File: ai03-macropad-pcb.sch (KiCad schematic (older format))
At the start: 74 parts, among them J1 Conn_01x06, SW1 SW_Push, U1 ATmega32U4-MU, Y1 16Mhz

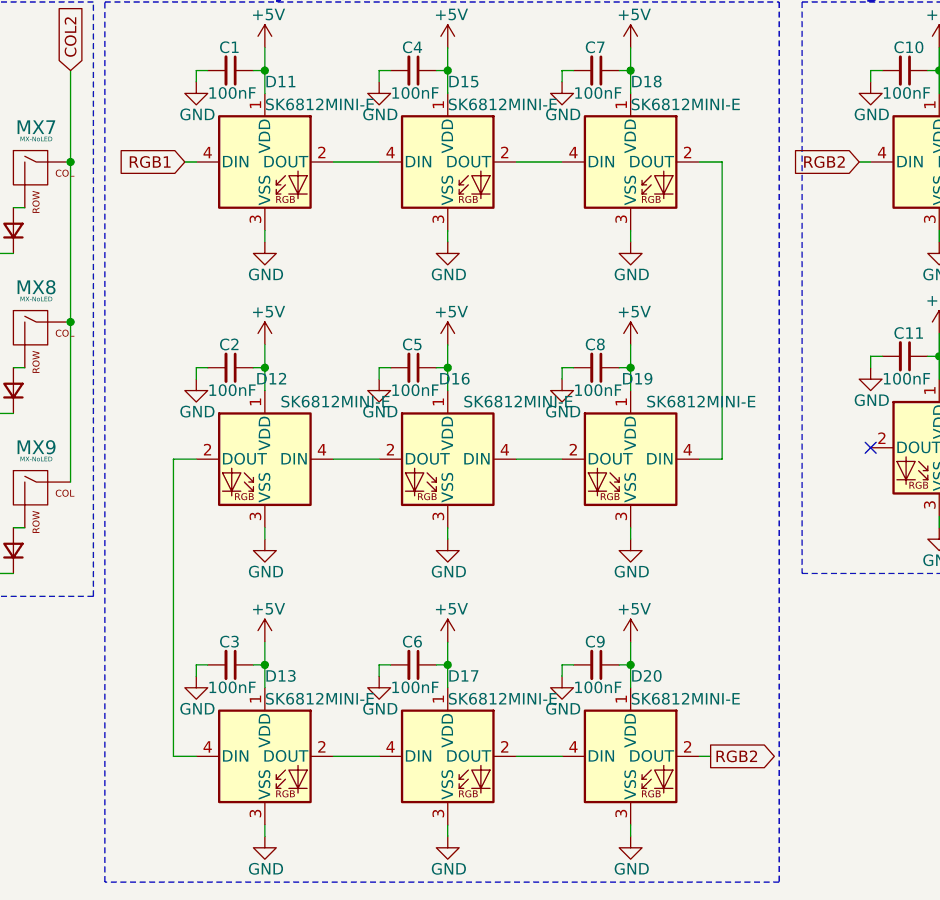
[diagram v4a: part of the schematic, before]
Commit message: Routing for switches and RGBs
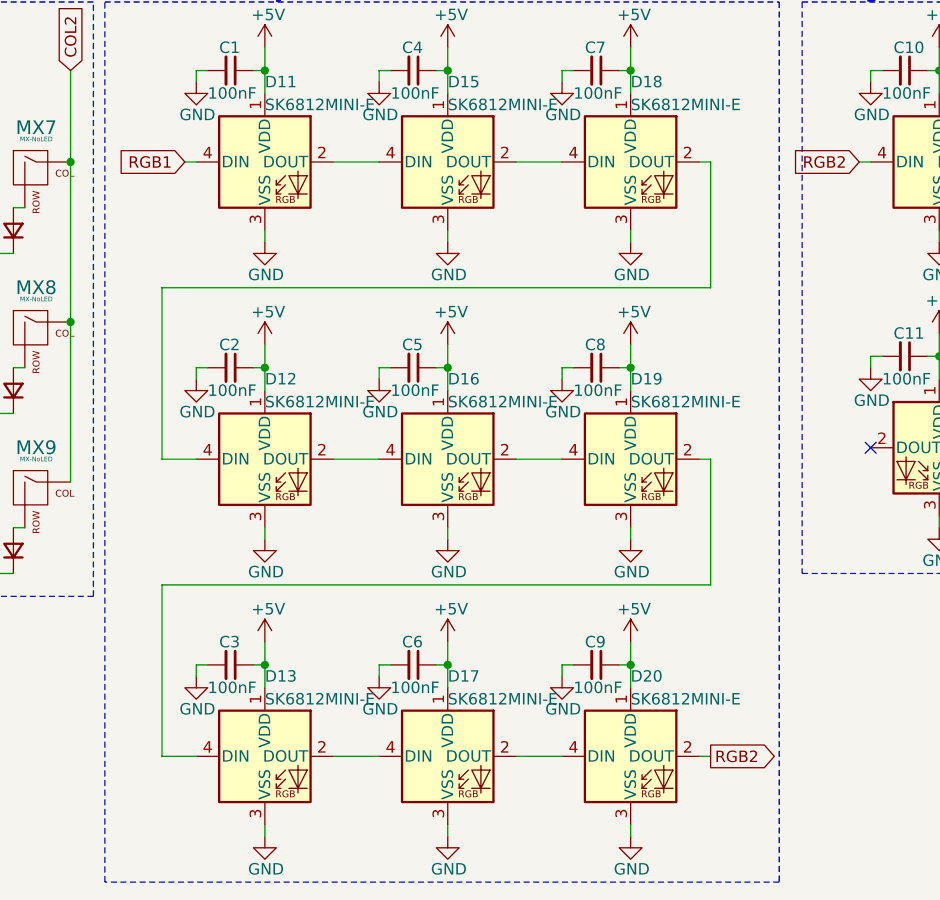
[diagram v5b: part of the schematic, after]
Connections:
- net at D18.2 (DOUT): now also D12.4 (DIN); no longer D19.4 (DIN)
- net at D19.2 (DOUT): now also D13.4 (DIN); no longer D16.4 (DIN)
- net at D16.2 (DOUT): now also D19.4 (DIN); no longer D12.4 (DIN)
- net at D12.2 (DOUT): now also D16.4 (DIN); no longer D13.4 (DIN)
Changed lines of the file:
@@
 	4400 4600 4600 4600
-Wire Wire Line
-	5200 4600 5300 4600
-Wire Wire Line
-	5300 4600 5300 5900
-Wire Wire Line
-	5300 5900 5200 5900
-Wire Wire Line
-	4600 5900 4400 5900
-Wire Wire Line
-	3800 5900 3600 5900
-Wire Wire Line
-	3000 5900 2900 5900
-Wire Wire Line
-	2900 5900 2900 7200
-Wire Wire Line
-	2900 7200 3000 7200
 Wire Wire Line
 	3600 7200 3800 7200
@@
 	1    4900 4600
 	1    0    0    -1
-$EndComp
-$Comp
-L kicad-keyboard-parts:SK6812MINI-E D19
-U 1 1 60741DD2
-P 4900 5900
-F 0 "D19" H 4800 6250 50  0000 L CNN
-F 1 "SK6812MINI-E" H 4350 6150 50  0000 L CNN
-F 2 "kicad-keyboard-parts:MX_SK6812MINI-E" H 4950 5600 50  0001 L TNN
-F 3 "https://cdn-shop.adafruit.com/product-files/2686/SK6812MINI_REV.01-1-2.pdf" H 5000 5525 50  0001 L TNN
-	1    4900 5900
-	-1   0    0    -1
-$EndComp
-$Comp
-L kicad-keyboard-parts:SK6812MINI-E D16
-U 1 1 60750D73
-P 4100 5900
-F 0 "D16" H 4000 6250 50  0000 L CNN
-F 1 "SK6812MINI-E" H 3550 6150 50  0000 L CNN
-F 2 "kicad-keyboard-parts:MX_SK6812MINI-E" H 4150 5600 50  0001 L TNN
-F 3 "https://cdn-shop.adafruit.com/product-files/2686/SK6812MINI_REV.01-1-2.pdf" H 4200 5525 50  0001 L TNN
-	1    4100 5900
-	-1   0    0    -1
-$EndComp
-$Comp
-L kicad-keyboard-parts:SK6812MINI-E D12
-U 1 1 60751636
-P 3300 5900
-F 0 "D12" H 3200 6250 50  0000 L CNN
-F 1 "SK6812MINI-E" H 2750 6150 50  0000 L CNN
-F 2 "kicad-keyboard-parts:MX_SK6812MINI-E" H 3350 5600 50  0001 L TNN
-F 3 "https://cdn-shop.adafruit.com/product-files/2686/SK6812MINI_REV.01-1-2.pdf" H 3400 5525 50  0001 L TNN
-	1    3300 5900
-	-1   0    0    -1
 $EndComp
 $Comp
@@
 Text GLabel 10750 6000 2    50   Input ~ 0
 ROW2
+$Comp
+L kicad-keyboard-parts:SK6812MINI-E D12
+U 1 1 60761311
+P 3300 5900
+F 0 "D12" H 3300 6250 50  0000 L CNN
+F 1 "SK6812MINI-E" H 3300 6150 50  0000 L CNN
+F 2 "kicad-keyboard-parts:MX_SK6812MINI-E" H 3350 5600 50  0001 L TNN
+F 3 "https://cdn-shop.adafruit.com/product-files/2686/SK6812MINI_REV.01-1-2.pdf" H 3400 5525 50  0001 L TNN
+	1    3300 5900
+	1    0    0    -1
+$EndComp
+$Comp
+L kicad-keyboard-parts:SK6812MINI-E D16
+U 1 1 6076131B
+P 4100 5900
+F 0 "D16" H 4100 6250 50  0000 L CNN
+F 1 "SK6812MINI-E" H 4100 6150 50  0000 L CNN
+F 2 "kicad-keyboard-parts:MX_SK6812MINI-E" H 4150 5600 50  0001 L TNN
+F 3 "https://cdn-shop.adafruit.com/product-files/2686/SK6812MINI_REV.01-1-2.pdf" H 4200 5525 50  0001 L TNN
+	1    4100 5900
+	1    0    0    -1
+$EndComp
+$Comp
+L kicad-keyboard-parts:SK6812MINI-E D19
+U 1 1 60761325
+P 4900 5900
+F 0 "D19" H 4900 6250 50  0000 L CNN
+F 1 "SK6812MINI-E" H 4900 6150 50  0000 L CNN
+F 2 "kicad-keyboard-parts:MX_SK6812MINI-E" H 4950 5600 50  0001 L TNN
+F 3 "https://cdn-shop.adafruit.com/product-files/2686/SK6812MINI_REV.01-1-2.pdf" H 5000 5525 50  0001 L TNN
+	1    4900 5900
+	1    0    0    -1
+$EndComp
+Wire Wire Line
+	5200 4600 5250 4600
+Wire Wire Line
+	5250 4600 5250 5150
+Wire Wire Line
+	5250 5150 2850 5150
+Wire Wire Line
+	2850 5150 2850 5900
+Wire Wire Line
+	2850 5900 3000 5900
+Wire Wire Line
+	3600 5900 3800 5900
+Wire Wire Line
+	4400 5900 4600 5900
+Wire Wire Line
+	5200 5900 5250 5900
+Wire Wire Line
+	5250 5900 5250 6450
+Wire Wire Line
+	5250 6450 2850 6450
+Wire Wire Line
+	2850 6450 2850 7200
+Wire Wire Line
+	2850 7200 3000 7200
 $EndSCHEMATC

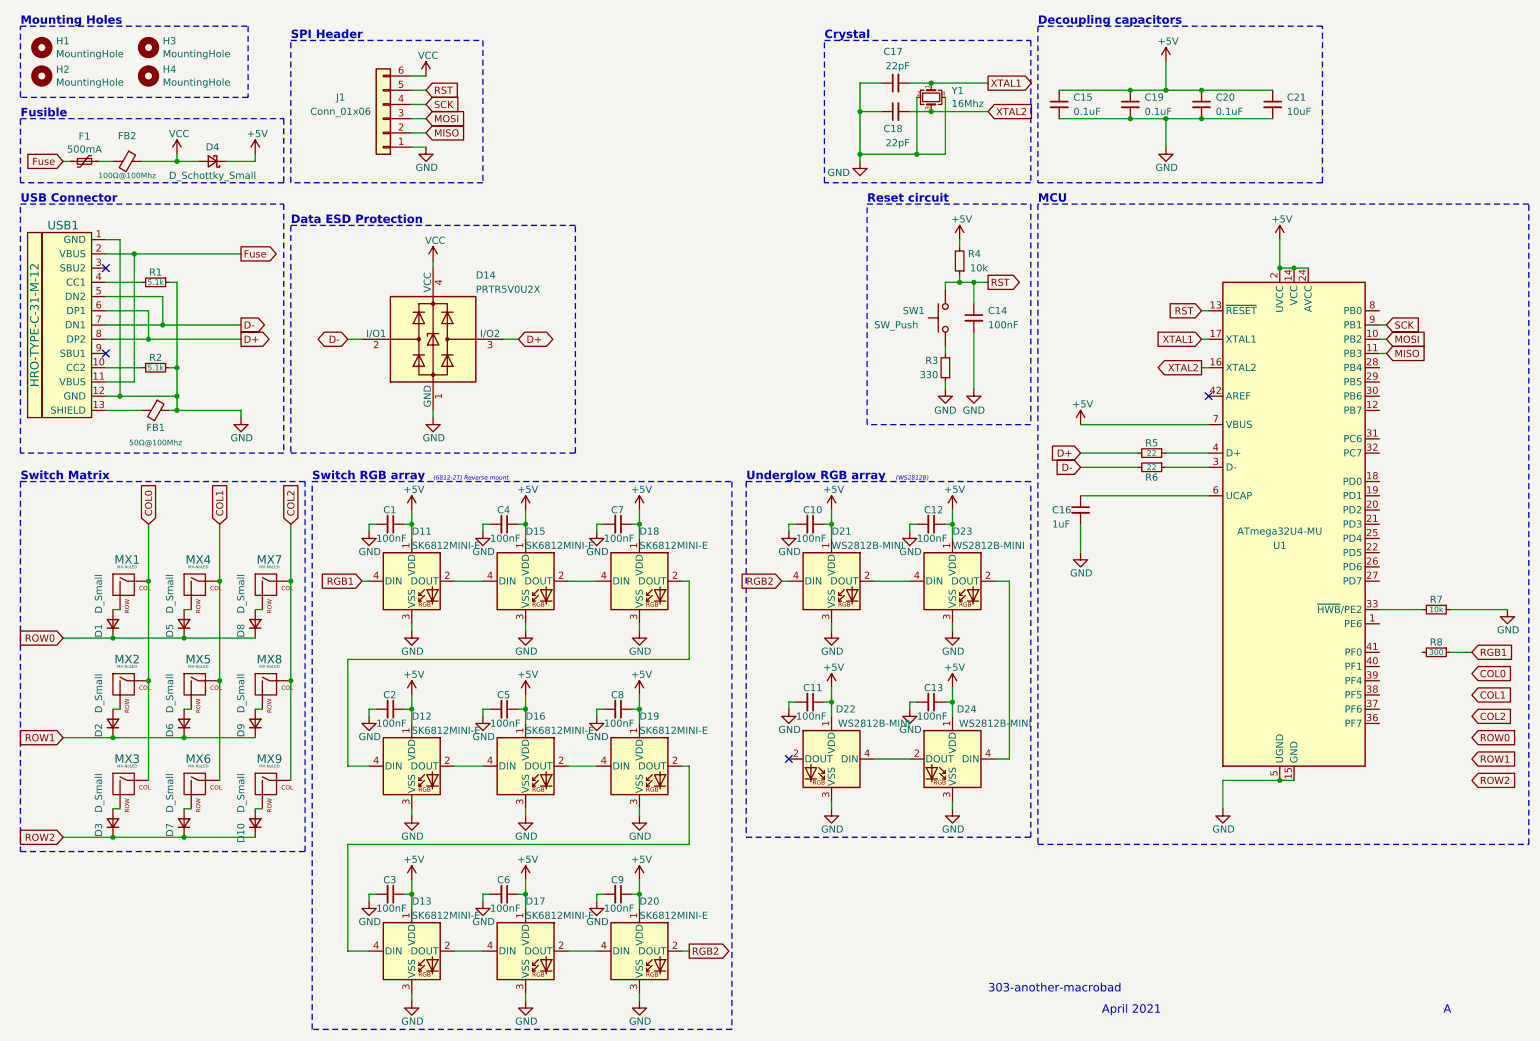
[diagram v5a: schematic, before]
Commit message: Routing of MCU, USB and BUS Lanes
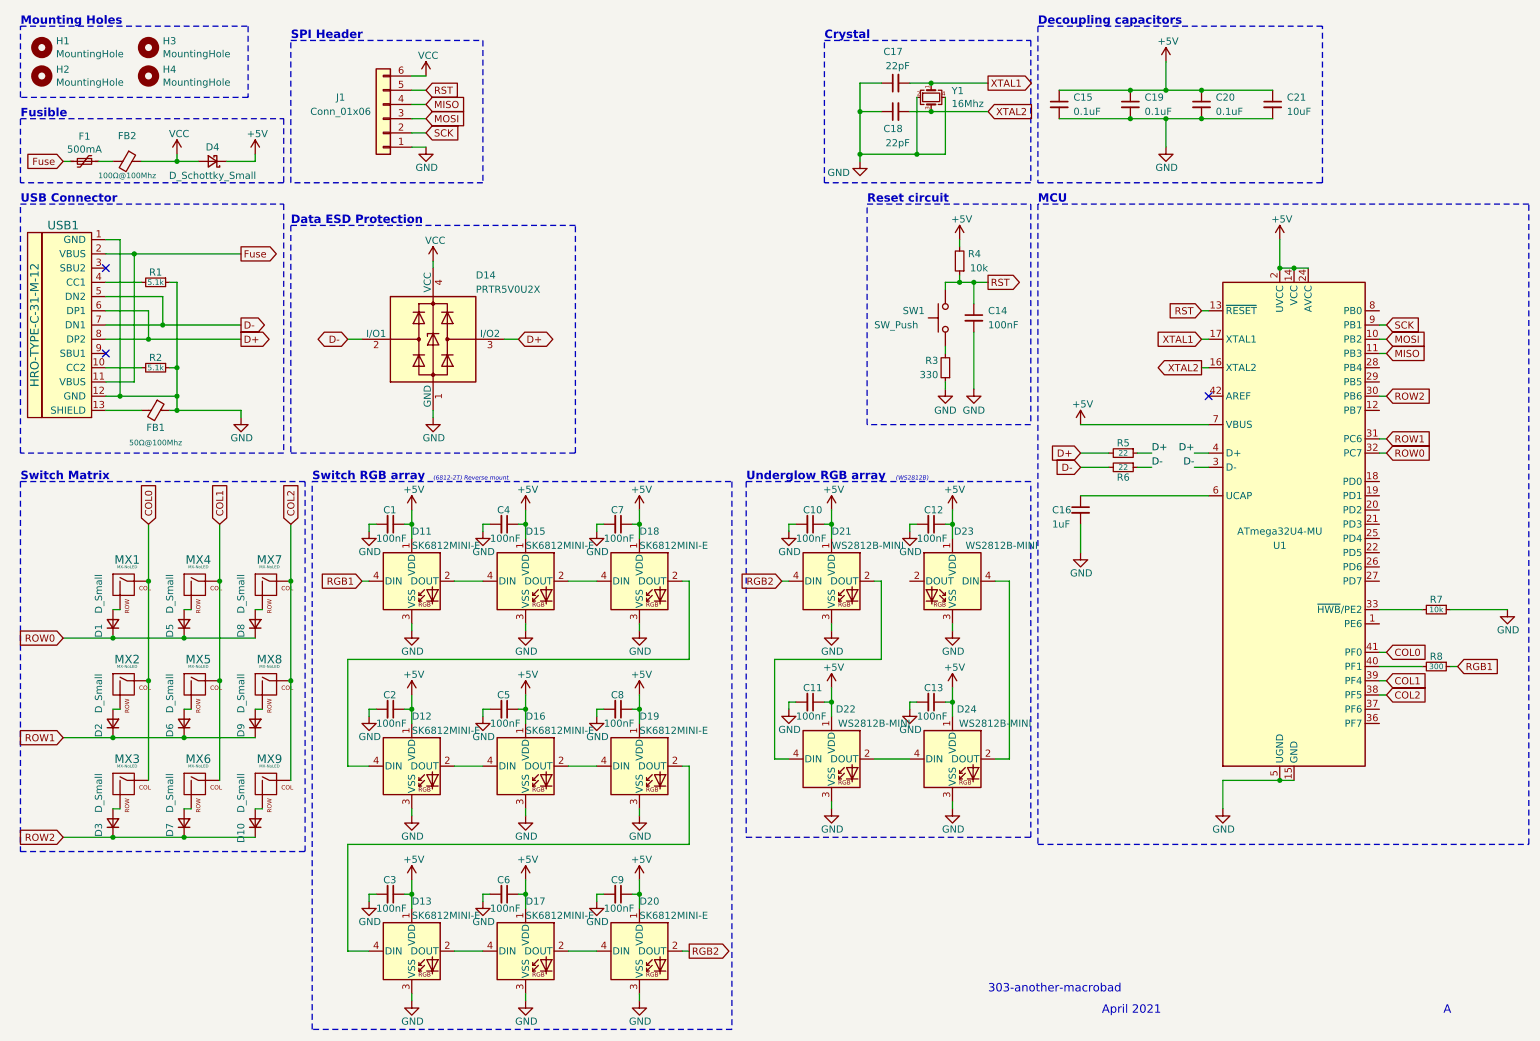
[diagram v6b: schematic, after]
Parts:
- J1: footprint Connector_JST:JST_SH_BM06B-SRSS-TB_1x06-1MP_P1.00mm_Vertical -> Connector_JST:JST_SHL_SM06B-SHLS-TF_1x06-1MP_P1.00mm_Horizontal
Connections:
- net COL0: now also U1.41 (PF0)
- net COL1: now also U1.39 (PF4)
- net COL2: now also U1.38 (PF5)
- net D+: now also R5.1, U1.4 (D+)
- net D-: now also R6.1, U1.3 (D-)
- net MISO: now also J1.4 (Pin_4); no longer J1.2 (Pin_2)
- net ROW0: now also U1.32 (PC7)
- net ROW1: now also U1.31 (PC6)
- net ROW2: now also U1.30 (PB6)
- net SCK: now also J1.2 (Pin_2); no longer J1.4 (Pin_4)
- net at U1.40 (PF1): now also R8.2
- net at D21.2 (DOUT): now also D22.4 (DIN); no longer D23.4 (DIN)
- net at D23.2 (DOUT): no longer D24.4 (DIN)
- net at D22.2 (DOUT): now also D24.4 (DIN)
- net at D24.2 (DOUT): now also D23.4 (DIN); no longer D22.4 (DIN)
- no-connect marks 4 -> 3
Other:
- moved on the sheet: R5, R6, R8
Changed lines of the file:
@@
 Connection ~ 1550 2800
-Wire Wire Line
-	1550 2800 2100 2800
-Wire Wire Line
-	1450 2900 2100 2900
 Wire Wire Line
 	1350 2300 2100 2300
@@
 	1    0    0    -1
 $EndComp
-Text GLabel 3400 1450 2    50   Input ~ 0
+Text GLabel 3400 1250 2    50   Input ~ 0
 MISO
 Text GLabel 3400 1350 2    50   Input ~ 0
 MOSI
-Text GLabel 3400 1250 2    50   Input ~ 0
+Text GLabel 3400 1450 2    50   Input ~ 0
 SCK
 Text GLabel 3400 1150 2    50   Input ~ 0
@@
 	10600 4800 11000 4800
 $Comp
-L Device:R_Small R5
-U 1 1 6072EE07
-P 8500 3700
-F 0 "R5" V 8400 3700 50  0000 C TNN
-F 1 "22" V 8500 3700 39  0000 C CNN
-F 2 "Resistor_SMD:R_0603_1608Metric" H 8500 3700 50  0001 C CNN
-F 3 "~" H 8500 3700 50  0001 C CNN
-	1    8500 3700
-	0    1    1    0
-$EndComp
-$Comp
-L Device:R_Small R6
-U 1 1 6073035A
-P 8500 3800
-F 0 "R6" V 8600 3800 50  0000 C BNN
-F 1 "22" V 8500 3800 39  0000 C CNN
-F 2 "Resistor_SMD:R_0603_1608Metric" H 8500 3800 50  0001 C CNN
-F 3 "~" H 8500 3800 50  0001 C CNN
-	1    8500 3800
-	0    1    1    0
-$EndComp
-Wire Wire Line
-	8900 3700 8600 3700
-Wire Wire Line
-	8900 3800 8600 3800
-Wire Wire Line
-	8400 3700 8000 3700
-$Comp
 L Device:C_Small C16
 U 1 1 6073582C
@@
 	1    0    0    -1
 $EndComp
-Wire Wire Line
-	8000 3800 8400 3800
 Wire Wire Line
 	8900 4000 8000 4000
@@
 Text GLabel 8850 2700 0    50   Input ~ 0
 RST
-Text GLabel 8000 3700 0    50   Input ~ 0
-D+
-Text GLabel 8000 3800 0    50   Input ~ 0
-D-
 $Comp
 L Device:C_Small C15
@@
 Wire Notes Line
 	11150 1950 7700 1950
-Wire Notes Line
-	7700 1950 7700 6450
 $Comp
 L power:+5V #PWR0123
@@
 $EndComp
 Wire Wire Line
-	6550 4600 6800 4600
-Wire Wire Line
 	850  6400 1200 6400
 Connection ~ 1200 6400
@@
 	1    0    0    -1
 $EndComp
-Wire Wire Line
-	6550 5850 6800 5850
-Wire Wire Line
-	7400 4600 7500 4600
-Wire Wire Line
-	7500 4600 7500 5850
-Wire Wire Line
-	7500 5850 7400 5850
-NoConn ~ 5950 5850
 Text Notes 5650 3900 0    59   ~ 12
 Underglow RGB array
@@
 U 1 1 60757A84
 P 7100 4600
-F 0 "D23" H 7100 4950 50  0000 L CNN
-F 1 "WS2812B-MINI" H 7100 4850 50  0000 L CNN
+F 0 "D23" H 6950 4950 50  0000 L CNN
+F 1 "WS2812B-MINI" H 6500 4850 50  0000 L CNN
 F 2 "LED_SMD:LED_SK6812MINI_PLCC4_3.5x3.5mm_P1.75mm" H 7150 4300 50  0001 L TNN
 F 3 "https://cdn-shop.adafruit.com/product-files/2686/SK6812MINI_REV.01-1-2.pdf" H 7200 4225 50  0001 L TNN
 	1    7100 4600
-	1    0    0    -1
+	-1   0    0    -1
 $EndComp
 $Comp
@@
 U 1 1 60758283
 P 6250 5850
-F 0 "D22" H 6150 6200 50  0000 C CNN
-F 1 "WS2812B-MINI" H 5950 6100 50  0000 C CNN
+F 0 "D22" H 6350 6200 50  0000 C CNN
+F 1 "WS2812B-MINI" H 6550 6100 50  0000 C CNN
 F 2 "LED_SMD:LED_SK6812MINI_PLCC4_3.5x3.5mm_P1.75mm" H 6300 5550 50  0001 L TNN
 F 3 "https://cdn-shop.adafruit.com/product-files/2686/SK6812MINI_REV.01-1-2.pdf" H 6350 5475 50  0001 L TNN
 	1    6250 5850
-	-1   0    0    -1
+	1    0    0    -1
 $EndComp
 $Comp
@@
 U 1 1 60769B15
 P 7100 5850
-F 0 "D24" H 7000 6200 50  0000 C CNN
-F 1 "WS2812B-MINI" H 6800 6100 50  0000 C CNN
+F 0 "D24" H 7200 6200 50  0000 C CNN
+F 1 "WS2812B-MINI" H 7400 6100 50  0000 C CNN
 F 2 "LED_SMD:LED_SK6812MINI_PLCC4_3.5x3.5mm_P1.75mm" H 7150 5550 50  0001 L TNN
 F 3 "https://cdn-shop.adafruit.com/product-files/2686/SK6812MINI_REV.01-1-2.pdf" H 7200 5475 50  0001 L TNN
 	1    7100 5850
-	-1   0    0    -1
+	1    0    0    -1
 $EndComp
 $Comp
@@
 F 0 "J1" H 3400 1200 50  0000 C CNN
 F 1 "Conn_01x06" H 3400 1300 50  0000 C CNN
-F 2 "Connector_JST:JST_SH_BM06B-SRSS-TB_1x06-1MP_P1.00mm_Vertical" H 3100 1350 50  0001 C CNN
+F 2 "Connector_JST:JST_SHL_SM06B-SHLS-TF_1x06-1MP_P1.00mm_Horizontal" H 3100 1350 50  0001 C CNN
 F 3 "~" H 3100 1350 50  0001 C CNN
 	1    3100 1350
@@
 L Device:R_Small R8
 U 1 1 607489F7
-P 10500 5100
-F 0 "R8" V 10400 5100 50  0000 C TNN
-F 1 "300" V 10500 5100 39  0000 C CNN
-F 2 "Resistor_SMD:R_0603_1608Metric" H 10500 5100 50  0001 C CNN
-F 3 "~" H 10500 5100 50  0001 C CNN
-	1    10500 5100
+P 10500 5200
+F 0 "R8" V 10400 5200 50  0000 C TNN
+F 1 "300" V 10500 5200 39  0000 C CNN
+F 2 "Resistor_SMD:R_0603_1608Metric" H 10500 5200 50  0001 C CNN
+F 3 "~" H 10500 5200 50  0001 C CNN
+	1    10500 5200
 	0    1    1    0
 $EndComp
-Text GLabel 10750 5100 2    50   Input ~ 0
+Text GLabel 10650 5200 2    50   Input ~ 0
 RGB1
-Wire Wire Line
-	10750 5100 10600 5100
-Text GLabel 10750 5250 2    50   Input ~ 0
+Text GLabel 10150 5100 2    50   Input ~ 0
 COL0
-Text GLabel 10750 5400 2    50   Input ~ 0
+Text GLabel 10150 5300 2    50   Input ~ 0
 COL1
-Text GLabel 10750 5550 2    50   Input ~ 0
+Text GLabel 10150 5400 2    50   Input ~ 0
 COL2
-Text GLabel 10750 5700 2    50   Input ~ 0
-ROW0
-Text GLabel 10750 5850 2    50   Input ~ 0
-ROW1
-Text GLabel 10750 6000 2    50   Input ~ 0
-ROW2
 $Comp
 L kicad-keyboard-parts:SK6812MINI-E D12
@@
 Wire Wire Line
 	2850 7200 3000 7200
+Wire Wire Line
+	1450 2900 2100 2900
+$Comp
+L Device:R_Small R6
+U 1 1 6073035A
+P 8300 3800
+F 0 "R6" V 8400 3800 50  0000 C BNN
+F 1 "22" V 8300 3800 39  0000 C CNN
+F 2 "Resistor_SMD:R_0603_1608Metric" H 8300 3800 50  0001 C CNN
+F 3 "~" H 8300 3800 50  0001 C CNN
+	1    8300 3800
+	0    1    1    0
+$EndComp
+Wire Wire Line
+	1550 2800 2100 2800
+$Comp
+L Device:R_Small R5
+U 1 1 6072EE07
+P 8300 3700
+F 0 "R5" V 8200 3700 50  0000 C TNN
+F 1 "22" V 8300 3700 39  0000 C CNN
+F 2 "Resistor_SMD:R_0603_1608Metric" H 8300 3700 50  0001 C CNN
+F 3 "~" H 8300 3700 50  0001 C CNN
+	1    8300 3700
+	0    1    1    0
+$EndComp
+Text GLabel 8000 3800 0    50   Input ~ 0
+D-
+Text GLabel 8000 3700 0    50   Input ~ 0
+D+
+Wire Notes Line
+	7700 1950 7700 6450
+Wire Wire Line
+	8000 3700 8200 3700
+Wire Wire Line
+	8000 3800 8200 3800
+Text GLabel 10150 3700 2    50   Input ~ 0
+ROW0
+Text GLabel 10150 3600 2    50   Input ~ 0
+ROW1
+Text GLabel 10150 3300 2    50   Input ~ 0
+ROW2
+Wire Wire Line
+	10150 3300 10100 3300
+Wire Wire Line
+	10150 3600 10100 3600
+Wire Wire Line
+	10150 3700 10100 3700
+Wire Wire Line
+	10150 5100 10100 5100
+Wire Wire Line
+	10100 5200 10400 5200
+Wire Wire Line
+	10600 5200 10650 5200
+Wire Wire Line
+	10150 5400 10100 5400
+Wire Wire Line
+	10150 5300 10100 5300
+Wire Wire Line
+	8400 3800 8500 3800
+Wire Wire Line
+	8400 3700 8500 3700
+Wire Wire Line
+	8900 3800 8800 3800
+Wire Wire Line
+	8900 3700 8800 3700
+Text Label 8800 3800 2    50   ~ 0
+D-
+Text Label 8800 3700 2    50   ~ 0
+D+
+Text Label 8500 3800 0    50   ~ 0
+D-
+Text Label 8500 3700 0    50   ~ 0
+D+
+Wire Wire Line
+	7400 4600 7500 4600
+Wire Wire Line
+	6550 5850 6800 5850
+Wire Wire Line
+	6550 4600 6600 4600
+Wire Wire Line
+	6600 4600 6600 5150
+Wire Wire Line
+	6600 5150 5850 5150
+Wire Wire Line
+	5850 5150 5850 5850
+Wire Wire Line
+	5850 5850 5950 5850
+Wire Wire Line
+	7400 5850 7500 5850
+Wire Wire Line
+	7500 5850 7500 4600
 $EndSCHEMATC
